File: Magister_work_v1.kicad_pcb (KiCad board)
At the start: 4 copper layers, 50.5 x 81 mm, 147 parts, among them J1 Conn_01x02_Pin, J10 Conn_01x06_Pin, J11 Conn_01x03_Pin, J12 Conn_01x03_Pin, J13 Conn_01x03_Pin, J14 Conn_01x03_Pin, J15 Conn_01x02_Pin, J17 Conn_01x04_Pin, J2 Conn_01x03_Pin, J3 Conn_01x03_Pin, J4 Conn_01x03_Pin, J5 Conn_01x03_Pin, J6 Conn_01x04_Pin, J7 Conn_01x02_Pin, J8 Conn_01x06_Pin, J9 Conn_01x02_Pin, Q1 AO3400A, Q2 AO3400A, U10 LSM6DS3, U11 MPU-6500, U12 BMI270, U2 XC6206P332MR, U3 Ai-Thinker-Ra-01, U4 MCP6001-OT, U5 AMS1117-3.3, U6 XL1509-5.0, U7 STM32F407VETx, U8 AT24C256, U9 Ai-Thinker-Ra-01SH, Y1 X322525MQB4SI, Y2 SMD03215C2

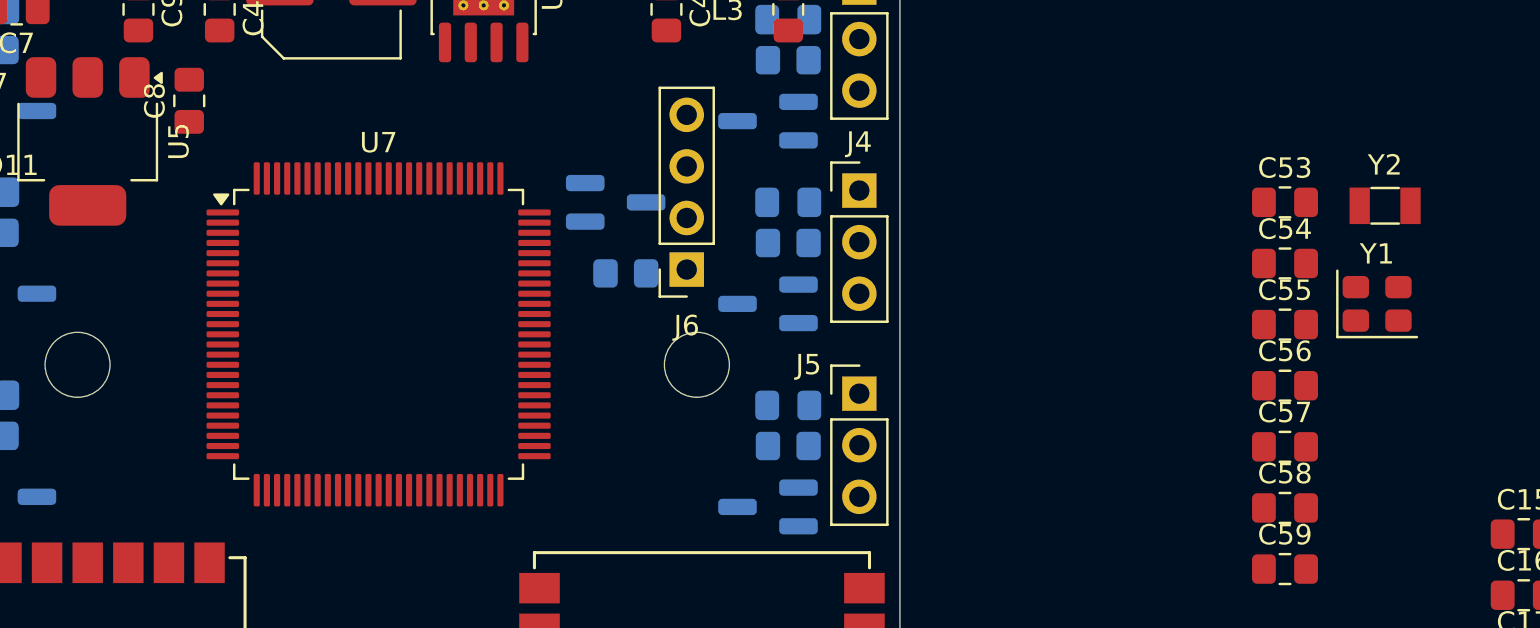
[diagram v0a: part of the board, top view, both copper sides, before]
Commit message: feat: добавлены все сигнальные линии к МК
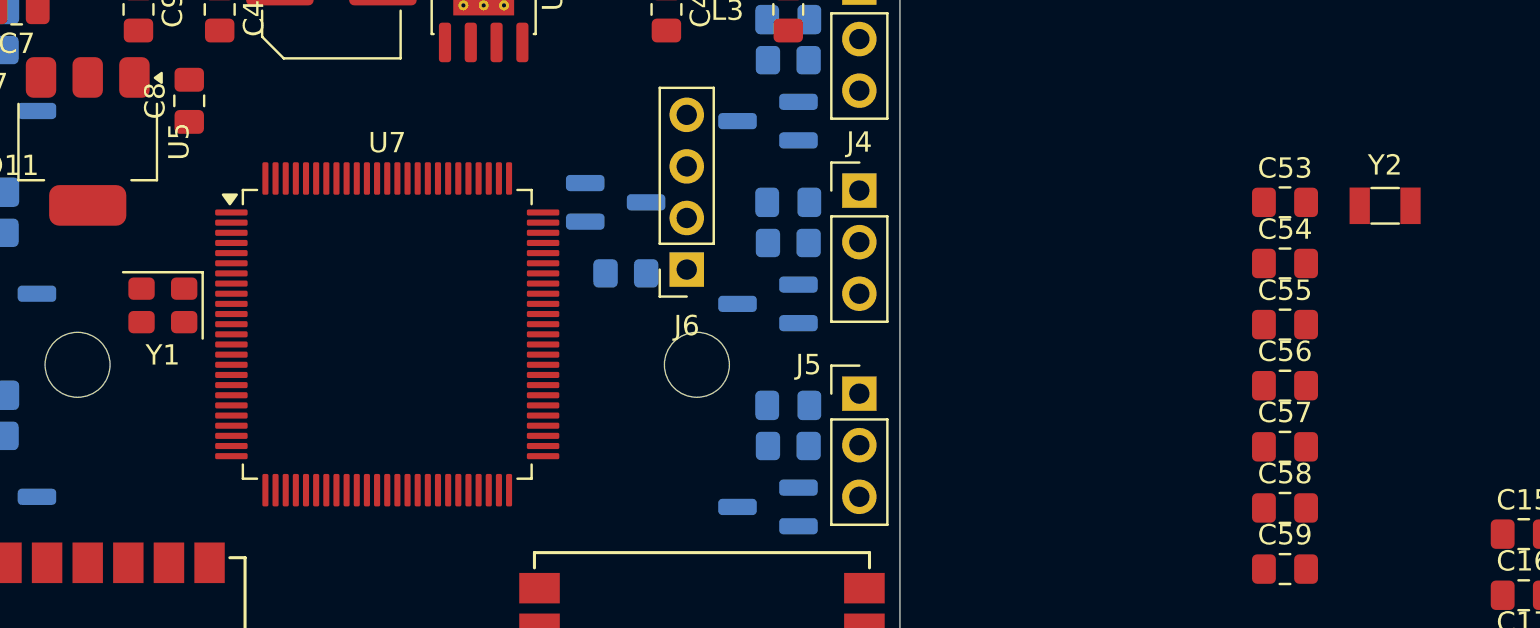
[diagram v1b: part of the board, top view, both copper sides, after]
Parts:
- moved Y1 59.8 mm to (44.2, 67.6), turned to 180 degrees
- moved U7 0.42 mm to (55.2, 69.0)
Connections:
- net Net-(U7-BOOT0) renamed /STMF401_Sheet/BOOT0
- net Net-(U7-NRST) renamed /STMF401_Sheet/RST
- net Net-(U7-VCAP_1) renamed /STMF401_Sheet/VCAP1
- net Net-(U7-VCAP_2) renamed /STMF401_Sheet/VCAP2
- DD3 pad 3: SDI_BMP280 -> LSM_SDI
- DD3 pad 4: SCK_BMP280 -> LSM_SCLK
- DD3 pad 5: SDO_BMP280 -> LSM_SDO
- U11 pad 23: MPU_SCLK -> BMI270_SCLK
- U11 pad 24: MPU_SDI -> BMI270_SDI
- U11 pad 9: MPU_SDO -> BMI270_SDO
- U7 pad 51: unconnected-(U7-PB12-Pad51) -> BMI270_CS
- U7 pad 52: unconnected-(U7-PB13-Pad52) -> BMI270_SCLK
- U7 pad 53: unconnected-(U7-PB14-Pad53) -> BMI270_SDO
- U7 pad 54: unconnected-(U7-PB15-Pad54) -> BMI270_SDI
- U7 pad 57: unconnected-(U7-PD10-Pad57) -> BMI270_INT1
- U7 pad 58: unconnected-(U7-PD11-Pad58) -> BMI270_INT2
- U7 pad 59: unconnected-(U7-PD12-Pad59) -> MPU_CS
- U7 pad 60: unconnected-(U7-PD13-Pad60) -> MPU_INT
- U7 pad 77: unconnected-(U7-PA15-Pad77) -> CSB_BMP280
- U7 pad 78: unconnected-(U7-PC10-Pad78) -> LSM_SCLK
- U7 pad 79: unconnected-(U7-PC11-Pad79) -> LSM_SDO
- U7 pad 80: unconnected-(U7-PC12-Pad80) -> LSM_SDI
- U7 pad 81: unconnected-(U7-PD0-Pad81) -> LSM_CS
- U7 pad 82: unconnected-(U7-PD1-Pad82) -> LSM_INT1
- U7 pad 83: unconnected-(U7-PD2-Pad83) -> LSM_INT2
- U7 pad 92: unconnected-(U7-PB6-Pad92) -> EEPROM_SCL
- U7 pad 93: unconnected-(U7-PB7-Pad93) -> EEPROM_SDA
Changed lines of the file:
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@@
 			(size 0.5 0.35)
 			(layers "F.Cu" "F.Mask" "F.Paste")
-			(net "SDI_BMP280")
+			(net "LSM_SDI")
 			(pinfunction "SDI_3")
 			(pintype "bidirectional")
@@
 			(size 0.5 0.35)
 			(layers "F.Cu" "F.Mask" "F.Paste")
-			(net "SCK_BMP280")
+			(net "LSM_SCLK")
 			(pinfunction "SCK_4")
 			(pintype "input")
@@
 			(size 0.5 0.35)
 			(layers "F.Cu" "F.Mask" "F.Paste")
-			(net "SDO_BMP280")
+			(net "LSM_SDO")
 			(pinfunction "SDO_5")
 			(pintype "bidirectional")
@@
 			(layers "F.Cu" "F.Mask" "F.Paste")
 			(roundrect_rratio 0.25)
-			(net "MPU_SDO")
+			(net "BMI270_SDO")
 			(pinfunction "AD0/SDO_9")
 			(pintype "bidirectional")
@@
 			(layers "F.Cu" "F.Mask" "F.Paste")
 			(roundrect_rratio 0.25)
-			(net "MPU_SCLK")
+			(net "BMI270_SCLK")
 			(pinfunction "SCL/SCLK_23")
 			(pintype "input")
@@
 			(layers "F.Cu" "F.Mask" "F.Paste")
 			(roundrect_rratio 0.25)
-			(net "MPU_SDI")
+			(net "BMI270_SDI")
 			(pinfunction "SDA/SDI_24")
 			(pintype "bidirectional")
@@
 		)
 		(property "Value" "SMD03215C2"
-			(at 0 2 0)
+			(at -62.235 12.235 180)
 			(layer "F.Fab")
 			(effects
@@
 	(footprint "Oscillator:Oscillator_SMD_Abracon_ASE-4Pin_3.2x2.5mm"
 		(layer "F.Cu")
-		(at 104 67.5)
+		(at 44.2 67.575 180)
 		(descr "Abracon ASE, Miniature Crystal Clock Oscillator, 3.2x2.5mm package, SMD, http://www.abracon.com/Oscillators/ASEseries.pdf")
 		(tags "SMD SMT crystal oscillator")
@@
 		(duplicate_pad_numbers_are_jumpers no)
 		(fp_line
-			(start -1.96 -1.635)
-			(end -1.96 1.635)
+			(start -1.96 1.635)
+			(end 1.96 1.635)
 			(stroke
 				(width 0.12)
@@
 		)
 		(fp_line
-			(start -1.96 1.635)
-			(end 1.96 1.635)
+			(start -1.96 -1.635)
+			(end -1.96 1.635)
 			(stroke
 				(width 0.12)
@@
 		)
 		(pad "1" smd roundrect
-			(at -1.05 0.825)
+			(at -1.05 0.825 180)
 			(size 1.3 1.1)
 			(layers "F.Cu" "F.Mask" "F.Paste")
@@
 		)
 		(pad "2" smd roundrect
-			(at 1.05 0.825)
+			(at 1.05 0.825 180)
 			(size 1.3 1.1)
 			(layers "F.Cu" "F.Mask" "F.Paste")
@@
 		)
 		(pad "3" smd roundrect
-			(at 1.05 -0.825)
+			(at 1.05 -0.825 180)
 			(size 1.3 1.1)
 			(layers "F.Cu" "F.Mask" "F.Paste")
@@
 		)
 		(pad "4" smd roundrect
-			(at -1.05 -0.825)
+			(at -1.05 -0.825 180)
 			(size 1.3 1.1)
 			(layers "F.Cu" "F.Mask" "F.Paste")
@@
 			(layers "F.Cu" "F.Mask" "F.Paste")
 			(roundrect_rratio 0.208333)
-			(net "Net-(U7-NRST)")
+			(net "/STMF401_Sheet/RST")
 			(pintype "passive")
 		)
@@
 			(layers "F.Cu" "F.Mask" "F.Paste")
 			(roundrect_rratio 0.212766)
-			(net "Net-(U7-VCAP_2)")
+			(net "/STMF401_Sheet/VCAP2")
 			(pintype "passive")
 		)
@@
 			(layers "F.Cu" "F.Mask" "F.Paste")
 			(roundrect_rratio 0.212766)
-			(net "Net-(U7-VCAP_1)")
+			(net "/STMF401_Sheet/VCAP1")
 			(pintype "passive")
 		)
@@
 			(layers "F.Cu" "F.Mask" "F.Paste")
 			(roundrect_rratio 0.208333)
-			(net "Net-(U7-BOOT0)")
+			(net "/STMF401_Sheet/BOOT0")
 			(pintype "passive")
 		)
@@
 	(footprint "Package_QFP:LQFP-100_14x14mm_P0.5mm"
 		(layer "F.Cu")
-		(at 54.825 69)
+		(at 55.25 69)
 		(descr "LQFP, 100 Pin (https://www.nxp.com/docs/en/package-information/SOT407-1.pdf)")
 		(tags "LQFP QFP")
@@
 			(layers "F.Cu" "F.Mask" "F.Paste")
 			(roundrect_rratio 0.25)
-			(net "Net-(U7-NRST)")
+			(net "/STMF401_Sheet/RST")
 			(pinfunction "NRST_14")
 			(pintype "input")
@@
 			(layers "F.Cu" "F.Mask" "F.Paste")
 			(roundrect_rratio 0.25)
-			(net "Net-(U7-VCAP_1)")
+			(net "/STMF401_Sheet/VCAP1")
 			(pinfunction "VCAP_1_49")
 			(pintype "power_out")
@@
 			(layers "F.Cu" "F.Mask" "F.Paste")
 			(roundrect_rratio 0.25)
-			(net "unconnected-(U7-PB12-Pad51)")
+			(net "BMI270_CS")
 			(pinfunction "PB12_51")
 			(pintype "bidirectional")
@@
 			(layers "F.Cu" "F.Mask" "F.Paste")
 			(roundrect_rratio 0.25)
-			(net "unconnected-(U7-PB13-Pad52)")
+			(net "BMI270_SCLK")
 			(pinfunction "PB13_52")
 			(pintype "bidirectional")
@@
 			(layers "F.Cu" "F.Mask" "F.Paste")
 			(roundrect_rratio 0.25)
-			(net "unconnected-(U7-PB14-Pad53)")
+			(net "BMI270_SDO")
 			(pinfunction "PB14_53")
 			(pintype "bidirectional")
@@
 			(layers "F.Cu" "F.Mask" "F.Paste")
 			(roundrect_rratio 0.25)
-			(net "unconnected-(U7-PB15-Pad54)")
+			(net "BMI270_SDI")
 			(pinfunction "PB15_54")
 			(pintype "bidirectional")
@@
 			(layers "F.Cu" "F.Mask" "F.Paste")
 			(roundrect_rratio 0.25)
-			(net "unconnected-(U7-PD10-Pad57)")
+			(net "BMI270_INT1")
 			(pinfunction "PD10_57")
 			(pintype "bidirectional")
@@
 			(layers "F.Cu" "F.Mask" "F.Paste")
 			(roundrect_rratio 0.25)
-			(net "unconnected-(U7-PD11-Pad58)")
+			(net "BMI270_INT2")
 			(pinfunction "PD11_58")
 			(pintype "bidirectional")
@@
 			(layers "F.Cu" "F.Mask" "F.Paste")
 			(roundrect_rratio 0.25)
-			(net "unconnected-(U7-PD12-Pad59)")
+			(net "MPU_CS")
 			(pinfunction "PD12_59")
 			(pintype "bidirectional")
@@
 			(layers "F.Cu" "F.Mask" "F.Paste")
 			(roundrect_rratio 0.25)
-			(net "unconnected-(U7-PD13-Pad60)")
+			(net "MPU_INT")
 			(pinfunction "PD13_60")
 			(pintype "bidirectional")
@@
 			(layers "F.Cu" "F.Mask" "F.Paste")
 			(roundrect_rratio 0.25)
-			(net "Net-(U7-VCAP_2)")
+			(net "/STMF401_Sheet/VCAP2")
 			(pinfunction "VCAP_2_73")
 			(pintype "power_out")
@@
 			(layers "F.Cu" "F.Mask" "F.Paste")
 			(roundrect_rratio 0.25)
-			(net "unconnected-(U7-PA15-Pad77)")
+			(net "CSB_BMP280")
 			(pinfunction "PA15_77")
 			(pintype "bidirectional")
@@
 			(layers "F.Cu" "F.Mask" "F.Paste")
 			(roundrect_rratio 0.25)
-			(net "unconnected-(U7-PC10-Pad78)")
+			(net "LSM_SCLK")
 			(pinfunction "PC10_78")
 			(pintype "bidirectional")
@@
 			(layers "F.Cu" "F.Mask" "F.Paste")
 			(roundrect_rratio 0.25)
-			(net "unconnected-(U7-PC11-Pad79)")
+			(net "LSM_SDO")
 			(pinfunction "PC11_79")
 			(pintype "bidirectional")
@@
 			(layers "F.Cu" "F.Mask" "F.Paste")
 			(roundrect_rratio 0.25)
-			(net "unconnected-(U7-PC12-Pad80)")
+			(net "LSM_SDI")
 			(pinfunction "PC12_80")
 			(pintype "bidirectional")
@@
 			(layers "F.Cu" "F.Mask" "F.Paste")
 			(roundrect_rratio 0.25)
-			(net "unconnected-(U7-PD0-Pad81)")
+			(net "LSM_CS")
 			(pinfunction "PD0_81")
 			(pintype "bidirectional")
@@
 			(layers "F.Cu" "F.Mask" "F.Paste")
 			(roundrect_rratio 0.25)
-			(net "unconnected-(U7-PD1-Pad82)")
+			(net "LSM_INT1")
 			(pinfunction "PD1_82")
 			(pintype "bidirectional")
@@
 			(layers "F.Cu" "F.Mask" "F.Paste")
 			(roundrect_rratio 0.25)
-			(net "unconnected-(U7-PD2-Pad83)")
+			(net "LSM_INT2")
 			(pinfunction "PD2_83")
 			(pintype "bidirectional")
@@
 			(layers "F.Cu" "F.Mask" "F.Paste")
 			(roundrect_rratio 0.25)
-			(net "unconnected-(U7-PB6-Pad92)")
+			(net "EEPROM_SCL")
 			(pinfunction "PB6_92")
 			(pintype "bidirectional")
@@
 			(layers "F.Cu" "F.Mask" "F.Paste")
 			(roundrect_rratio 0.25)
-			(net "unconnected-(U7-PB7-Pad93)")
+			(net "EEPROM_SDA")
 			(pinfunction "PB7_93")
 			(pintype "bidirectional")
@@
 			(layers "F.Cu" "F.Mask" "F.Paste")
 			(roundrect_rratio 0.25)
-			(net "Net-(U7-BOOT0)")
+			(net "/STMF401_Sheet/BOOT0")
 			(pinfunction "BOOT0_94")
 			(pintype "input")
@@
 			(layers "F.Cu" "F.Mask" "F.Paste")
 			(roundrect_rratio 0.212766)
-			(net "Net-(U7-NRST)")
+			(net "/STMF401_Sheet/RST")
 			(pintype "passive")
 		)

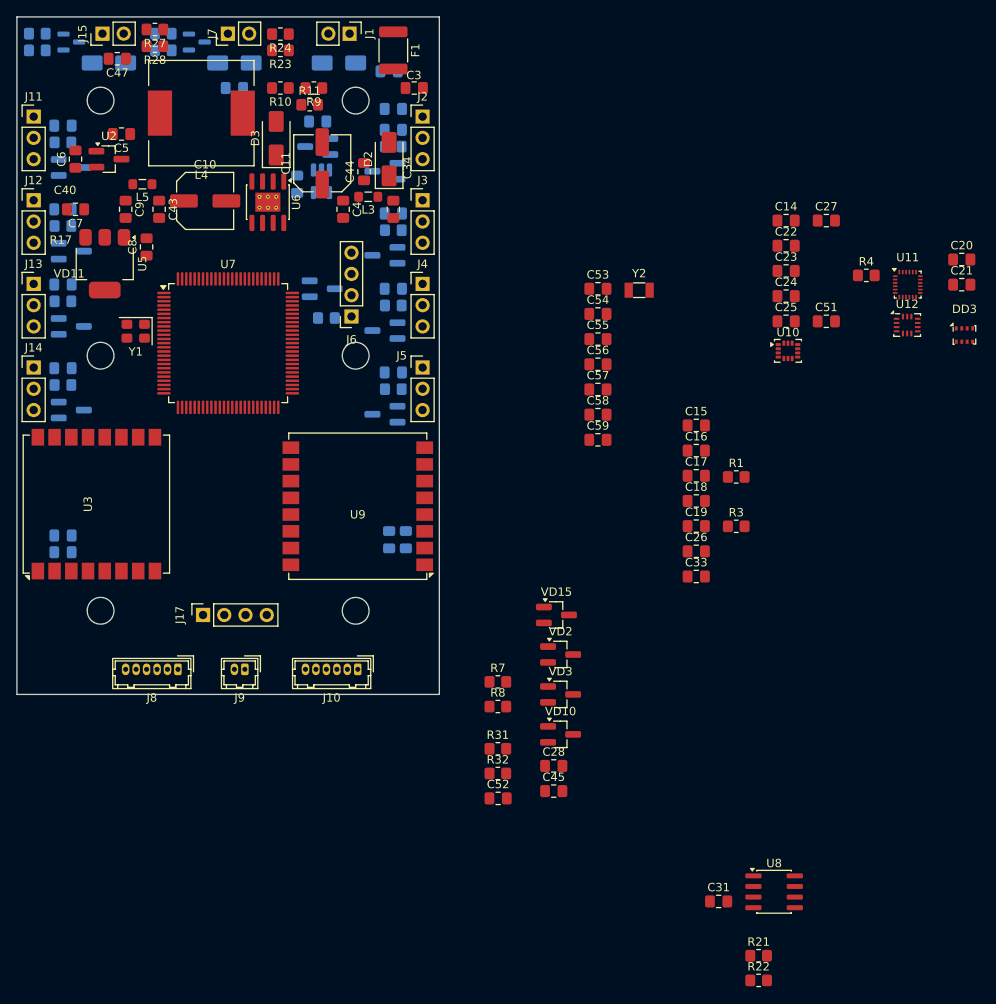
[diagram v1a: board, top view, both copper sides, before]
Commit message: feat: добавлены светодиоды, размещены почти все компоненты кроме модулей IMU
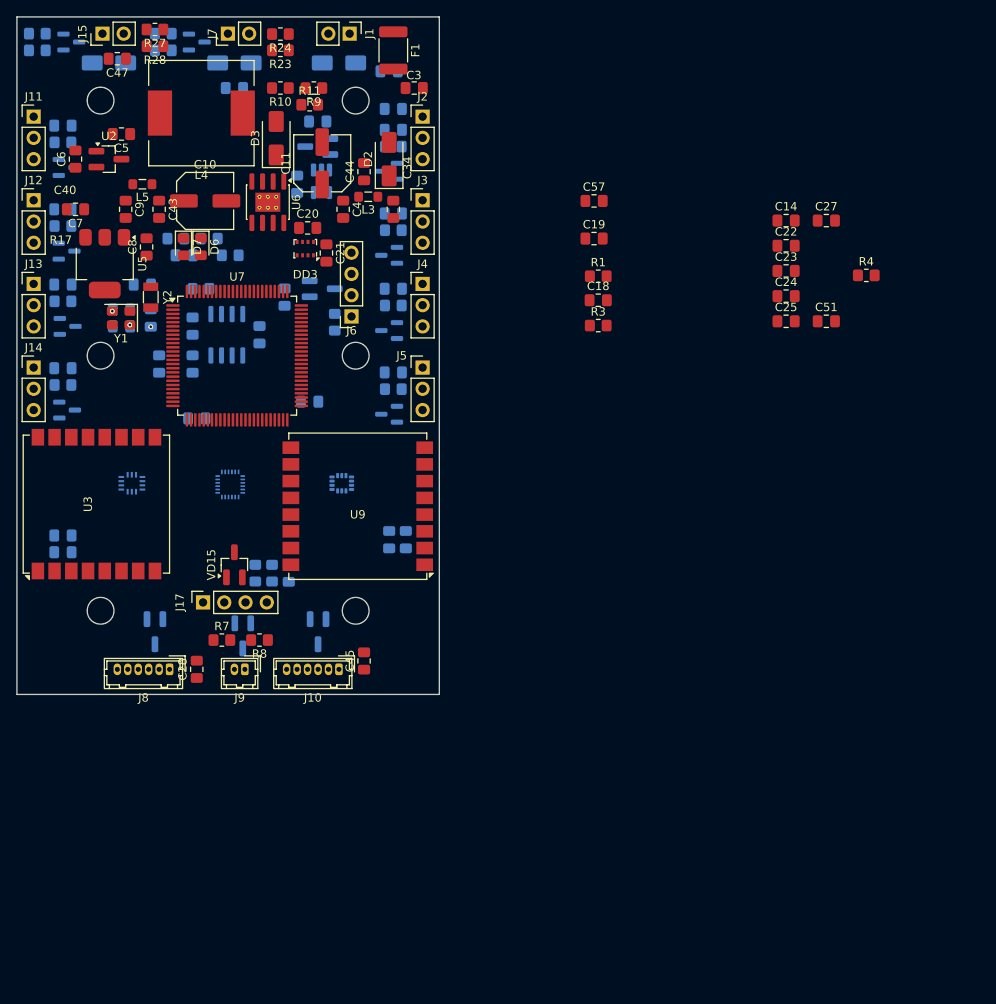
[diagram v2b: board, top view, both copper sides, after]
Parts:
- added D6: LED, LED_SMD:LED_0805_2012Metric_Pad1.15x1.40mm_HandSolder, F.Cu at (52.0, 57.5)
- added D7: LED, LED_SMD:LED_0805_2012Metric_Pad1.15x1.40mm_HandSolder, F.Cu at (49.9, 57.5)
- added R2: 330, Resistor_SMD:R_0805_2012Metric_Pad1.20x1.40mm_HandSolder, B.Cu at (53.0, 56.5)
- added R5: 330, Resistor_SMD:R_0805_2012Metric_Pad1.20x1.40mm_HandSolder, B.Cu at (49.0, 56.5)
- C15, C16, C17, C26, C31, C33, C52, C53, C54, C55, C56, C58, C59, R21, R22, R31, R32, U10, U11, U12, U8, VD10, VD2, VD3: moved to B.Cu
- VD11, VD12, VD13, VD5, VD6, VD7, VD8, VD9: footprint Package_TO_SOT_SMD:SOT-23_Handsoldering -> Package_TO_SOT_SMD:SOT-23
- moved R22 106.2 mm to (52.0, 62.5)
- moved R21 104.9 mm to (55.5, 58.5), turned to 180 degrees
- moved U12 94.6 mm to (43.7, 85.8), turned to 180 degrees
- moved U8 93.4 mm to (55.1, 68.0), turned to 90 degrees
- moved C31 87.2 mm to (59.0, 68.0), turned to -90 degrees
- moved U11 84.5 mm to (55.5, 85.9), turned to 180 degrees
- moved DD3 79.5 mm to (64.5, 57.7), turned to 180 degrees
- moved C20 78.3 mm to (64.8, 55.2)
- moved C21 76.1 mm to (67.0, 58.2), turned to -90 degrees
- moved C26 68.0 mm to (47.0, 71.5), turned to -90 degrees
- moved C33 67.3 mm to (51.0, 67.0), turned to 90 degrees
- moved C17 60.1 mm to (51.5, 78.0), turned to 180 degrees
- moved Y2 58.4 mm to (46.0, 63.5), turned to -90 degrees
- moved C59 57.5 mm to (45.0, 62.0), turned to 180 degrees
- moved C56 57.1 mm to (42.5, 67.0)
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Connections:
- U7 pad 1: unconnected-(U7-PE2-Pad1) -> Net-(D7-A)
- U7 pad 98: unconnected-(U7-PE1-Pad98) -> Net-(D6-A)
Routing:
- net GND: vias 0 -> 3
